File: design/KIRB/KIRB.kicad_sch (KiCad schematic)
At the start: 32 parts, among them J1 3S Balance Connector, J2 USB_B_Micro, J3 J_IN1/J_IN3, J4 J_IN4/J_IN2, M1 Motor_DC, M2 Motor_DC, SW1 Power Switch, U1 DC-DC Buck Converter Module, U10 36-Pos Quadrature Encoder, U17 SN74LVC245A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

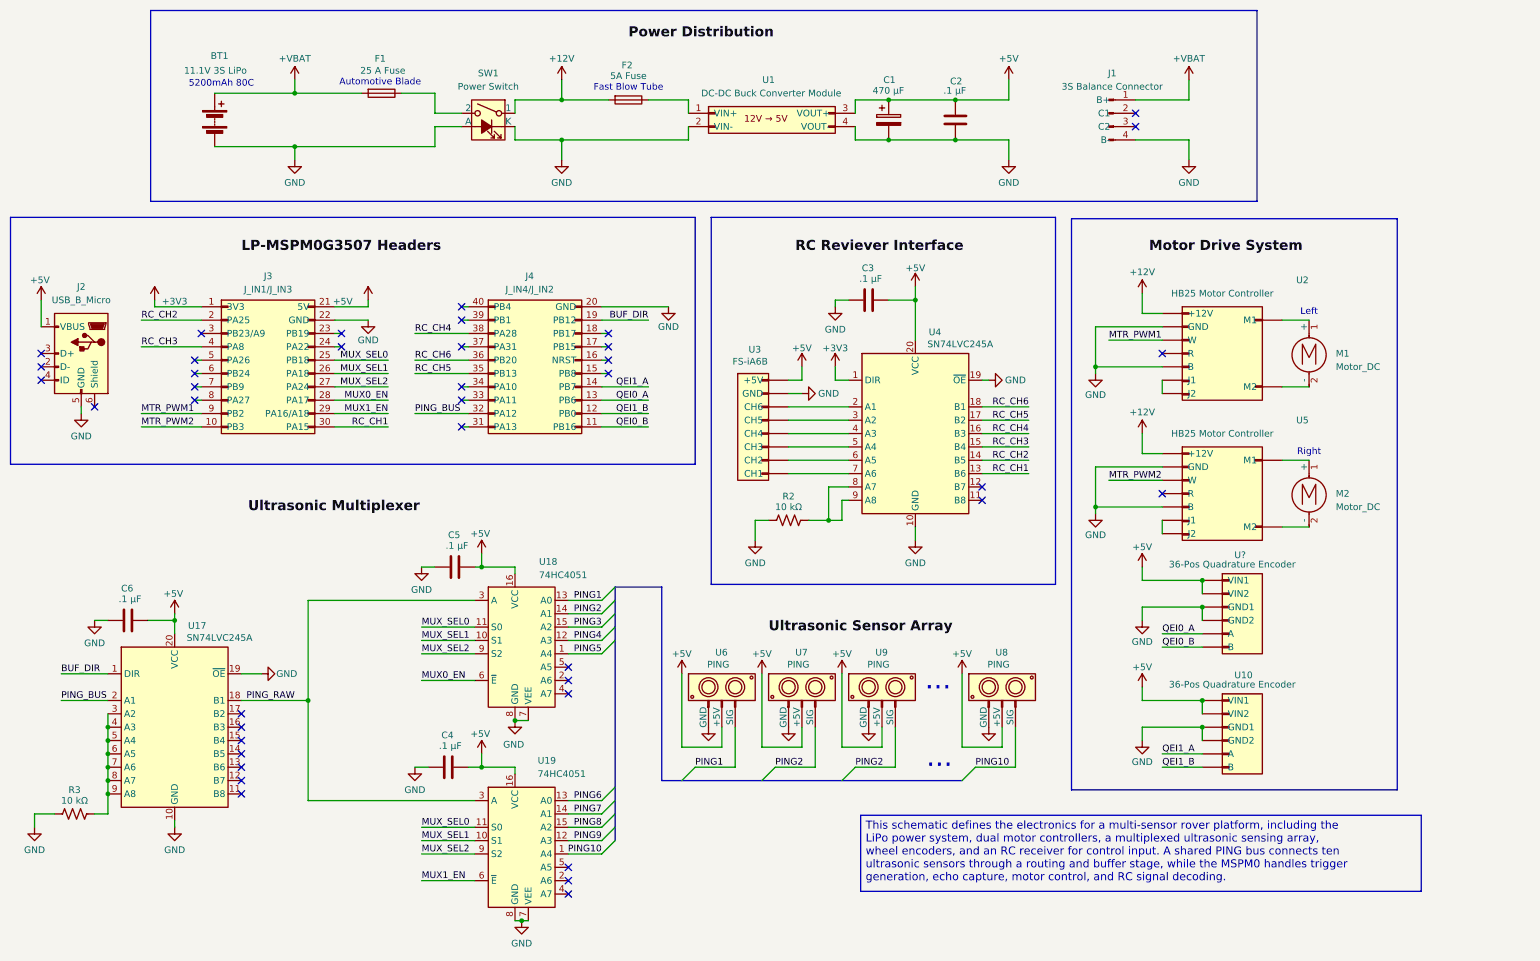
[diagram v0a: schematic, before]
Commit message: kicad system block diagram and pin reassignment
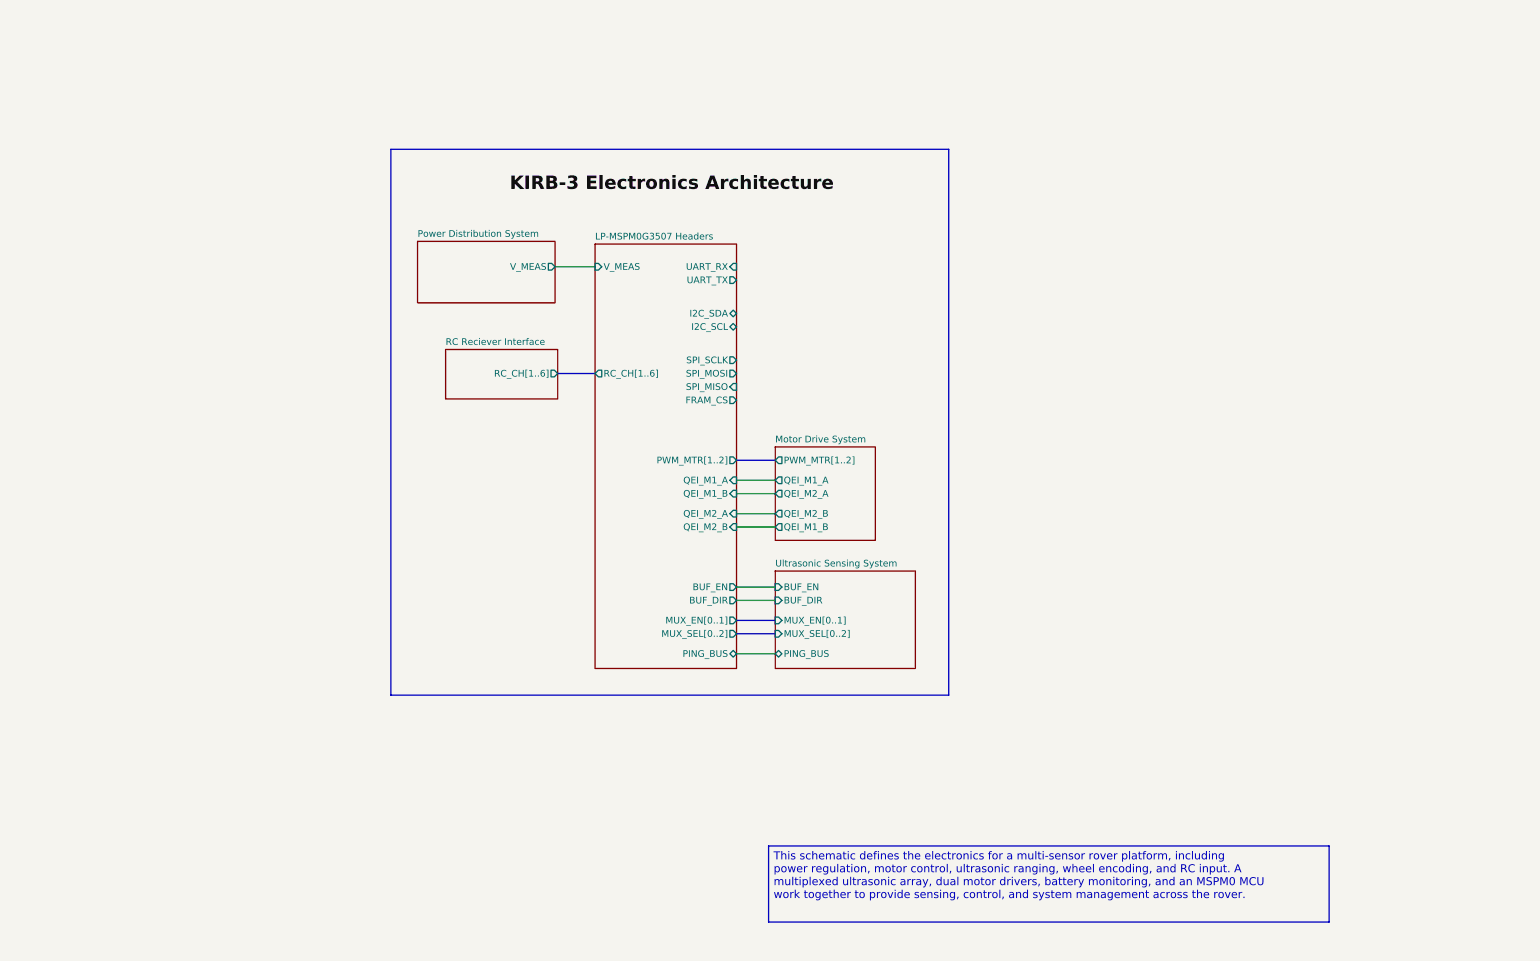
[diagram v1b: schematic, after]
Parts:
- removed BT1: 11.1V 3S LiPo, symbol Device:Battery
- removed C1: 470 µF, symbol Device:C_Polarized
- removed C2, C3, C4, C5, C6: .1 µF, symbol Device:C
- removed F1: 25 A Fuse, symbol Device:Fuse
- removed F2: 5A Fuse, symbol Device:Fuse
- removed J1: 3S Balance Connector, symbol Connector:Conn_01x04_Pin
- removed J2: USB_B_Micro, symbol Connector:USB_B_Micro
- removed J3: J_IN1/J_IN3, Connector_PinHeader_2.54mm:PinHeader_2x10_P2.54mm_Vertical, symbol Connector_Generic:Conn_02x10_Counter_Clockwise
- removed J4: J_IN4/J_IN2, Connector_PinHeader_2.54mm:PinHeader_2x10_P2.54mm_Vertical, symbol Connector_Generic:Conn_02x10_Counter_Clockwise
- removed M1, M2: Motor_DC, symbol Motor:Motor_DC
- removed R2, R3: 10 kΩ, symbol Device:R_US
- removed SW1: Power Switch, symbol Switch:SW_SPST_LED
- removed U1: DC-DC Buck Converter Module, symbol Connector_Generic:Conn_02x02_Top_Bottom
- removed U10, U?: 36-Pos Quadrature Encoder, symbol Connector_Generic:Conn_01x06
- removed U17, U4: SN74LVC245A, Package_SO:TSSOP-20_4.4x6.5mm_P0.65mm, symbol Logic_LevelTranslator:SN74LVC245APW
- removed U18, U19: 74HC4051, symbol 74xx:74HC4051
- removed U2, U5: HB25 Motor Controller, symbol Connector_Generic:Conn_02x04_Odd_Even
- removed U3: FS-iA6B, symbol Connector_Generic:Conn_01x08
- removed U6, U7, U8, U9: PING, symbol Connector_Generic:Conn_01x03
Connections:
- no-connect marks 40 -> 0
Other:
- added sheet LP-MSPM0G3507 Headers (LP_MSPM0G3507_HDR.kicad_sch)
- added sheet Motor Drive System (MOTOR_IF.kicad_sch)
- added sheet Power Distribution System (POWER.kicad_sch)
- added sheet RC Reciever Interface (RC_RECV_IF.kicad_sch)
- added sheet Ultrasonic Sensing System (ULTRASONICS.kicad_sch)
- note removed: "..."
- note removed: "5200mAh 80C"
- note removed: "Automotive Blade"
- note removed: "Fast Blow Tube"
- note removed: "Left"
- note removed: "Right"
